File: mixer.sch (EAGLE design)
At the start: 53 parts, among them J1 SJ-3502-SMT-TR, Q1 2SCR574D3TL1, Q2 2SCR574D3TL1, U1 MCP1703T-5002E, U2 SA602AD8-SOIC, U3 LM386M-1, X1 Antenna, Y1 7.040MHz

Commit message: splitting boards, doing layouts
Split into two boards with jumpers between. Added jumper for crystal to be able to change reference frequency. Closer to real layouts, still need to solidify some parts.
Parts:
- removed C1: 0.1U, adafruit:C-USC0805
- removed C10, C12, C18: 150p, adafruit:C-USC0805
- removed C11, C16, C17, C19, C2: 10n, adafruit:C-USC0805
- removed C22: 33u/16V, adafruit:C-USC0805
- removed C23, C24, C25: 10u/16V, adafruit:C-USC0805
- removed C5: 0.1u, adafruit:C-USC0805
- removed C6, C7: 390p, adafruit:C-USC0805
- removed C8: 680p, adafruit:C-USC0805
- removed C9: 100p, adafruit:C-USC0805
- removed J1: SJ-3502-SMT-TR, Audio Connectors:SJ-3502-SMT-TR
- removed L2: 470uH, MLF2012E5R6KT000:MLF2012E5R6KT000
- removed L3: 5.6uH, MLF2012E5R6KT000:MLF2012E5R6KT000
- removed L4: 16uH, MLF2012E5R6KT000:MLF2012E5R6KT000
- removed L5: 1.2uH, MLF2012E5R6KT000:MLF2012E5R6KT000
- removed Q1, Q2: 2SCR574D3TL1, zort2:2SCR574D3TL1
- removed R1, R2: 1k, pot:TRIM_EU-3223G
- removed R6: 6.8K, adafruit:R-US_M0805
- removed R7: 100, adafruit:R-US_M0805
- removed U1: MCP1703T-5002E, linear:MCP170312MB
- removed U3: LM386M-1, linear:LM386M-1
- removed VIN: AB9V, battery:AB9V
- removed X1: Antenna, adafruit:SMACONNECTOR_EDGE
- removed Y1: 7.040MHz, adafruit:CRYSTALCTS406
- added CRYSTAL: (no value), adafruit:PINHD-1X3
- added JP1: (no value), adafruit:PINHD-2X4
- R4: value 1.5K -> 1k; device adafruit:R-US_M0805 -> zort2:3362W-1-102LF
- R5: value 6.8K -> 25K; device adafruit:R-US_M0805 -> zort2:3362W-1-102LF
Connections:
- removed net HEADPHONE: C24.2, J1.2
- removed net KEY_IN: J1.3, R4.1
- removed net N$10: C17.2, U3.-IN
- removed net N$11: C23.1, U3.BYPASS
- removed net N$12: C25.1, U3.GAIN@2
- removed net N$13: C25.2, U3.GAIN@1
- removed net N$14: C24.1, U3.OUT
- removed net N$19: C12.2, Q1.1, R5.2, R6.1
- removed net N$20: C11.1, Q1.3, R4.2
- removed net N$21: C18.1, L3.1, Q1.2
- removed net N$22: C10.1, C18.2, R7.1
- removed net N$23: L2.2, Q2.1, R7.2
- removed net N$24: C19.1, L4.1, Q2.2
- removed net N$25: C19.2, C8.1, C9.1, L5.1
- removed net N$26: C6.1, C7.1, L5.2, X1.ANT
- removed net N$9: C16.2, U3.+IN
- net 6V_DC: now also JP1.5, R5.1; no longer C2.1, R2.E, U1.VO
- net ANT_IN: now also JP1.1; no longer C9.2
- net ANT_OUT: now also JP1.2; no longer C12.1
- net GND: now also JP1.8, R4.3, R5.3; no longer C1.2, C10.2, C11.2, C2.2, C22.2, C23.2, C6.2, C7.2, C8.2, J1.1, L2.1, Q2.3, R1.A, R2.A, R5.1, U1.GND, U3.GND, VIN.-, X1.GND1, X1.GND2, X1.GND3, X1.GND4
- net N$15: now also CRYSTAL.1; no longer Y1.1
- net N$18: now also R5.2; no longer R2.S
- net N$4: now also CRYSTAL.3; no longer Y1.2
- net N$5: now also R4.2; no longer R1.S
- net N$6: now also R4.1; no longer R1.E
- net OUT_A: now also JP1.3; no longer C16.1, C5.1
- net OUT_B: now also JP1.4; no longer C17.1, C5.2
- net VIN: now also JP1.7; no longer C1.1, C22.1, L3.2, L4.2, R6.2, U1.VI1, U3.VS, VIN.+
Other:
- note added: "7.040 MHz"
- note removed: "Audio I/O"
- note removed: "Power Supply"
- moved on the sheet: C13, C14, C15, C20, C21, C26, C3, C4, D1, D2, D3, L1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

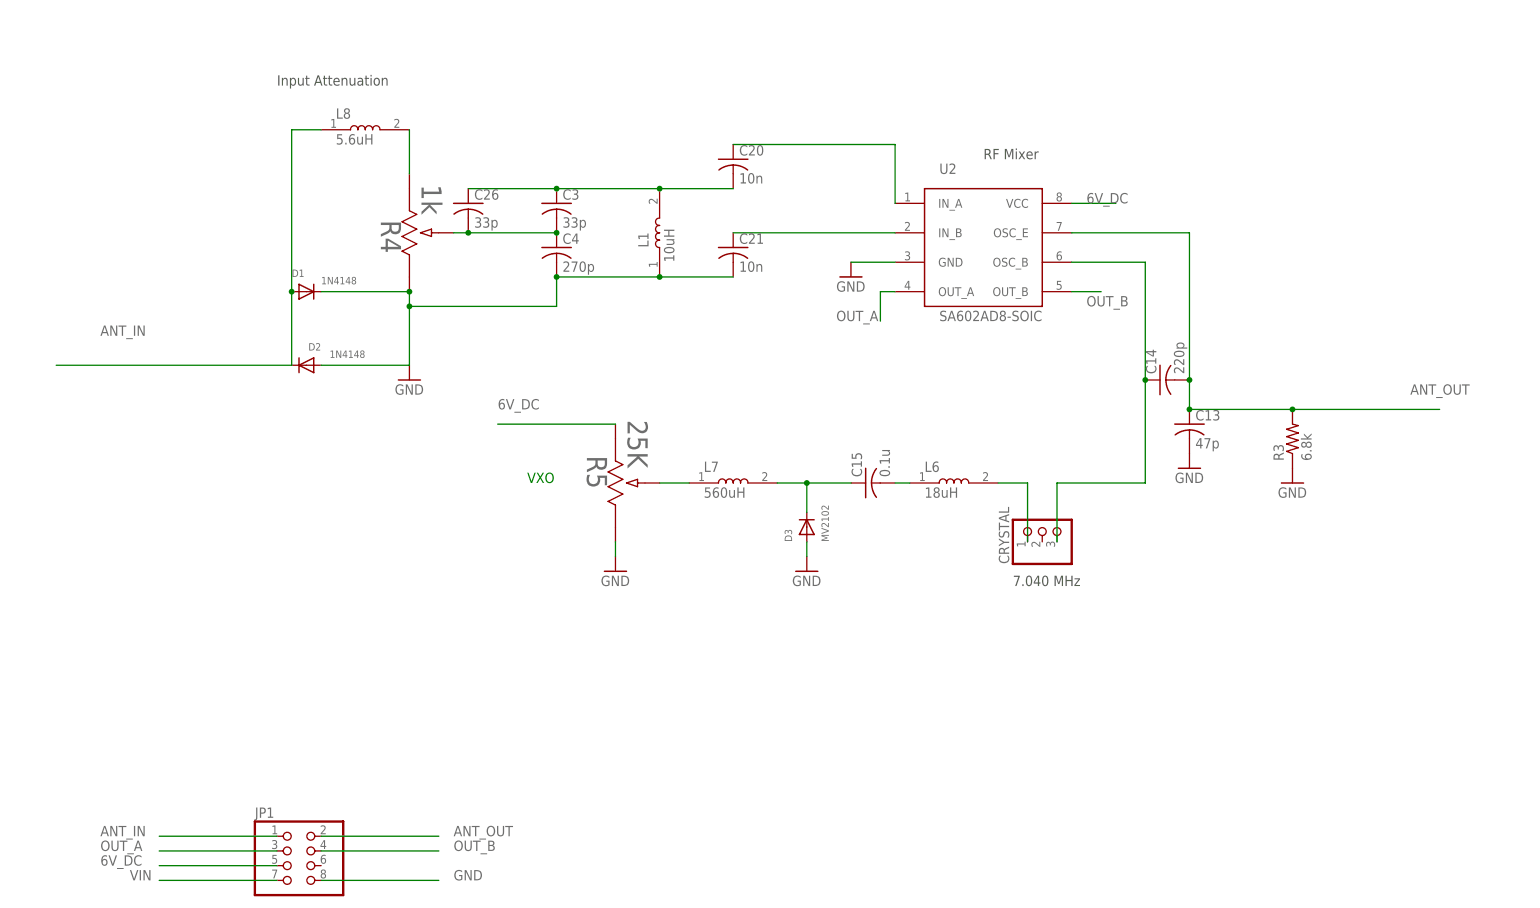
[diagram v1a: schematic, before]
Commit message: forgot to save mixer schematic
Forgot to save while adjusting the schematic layout to make it more readable
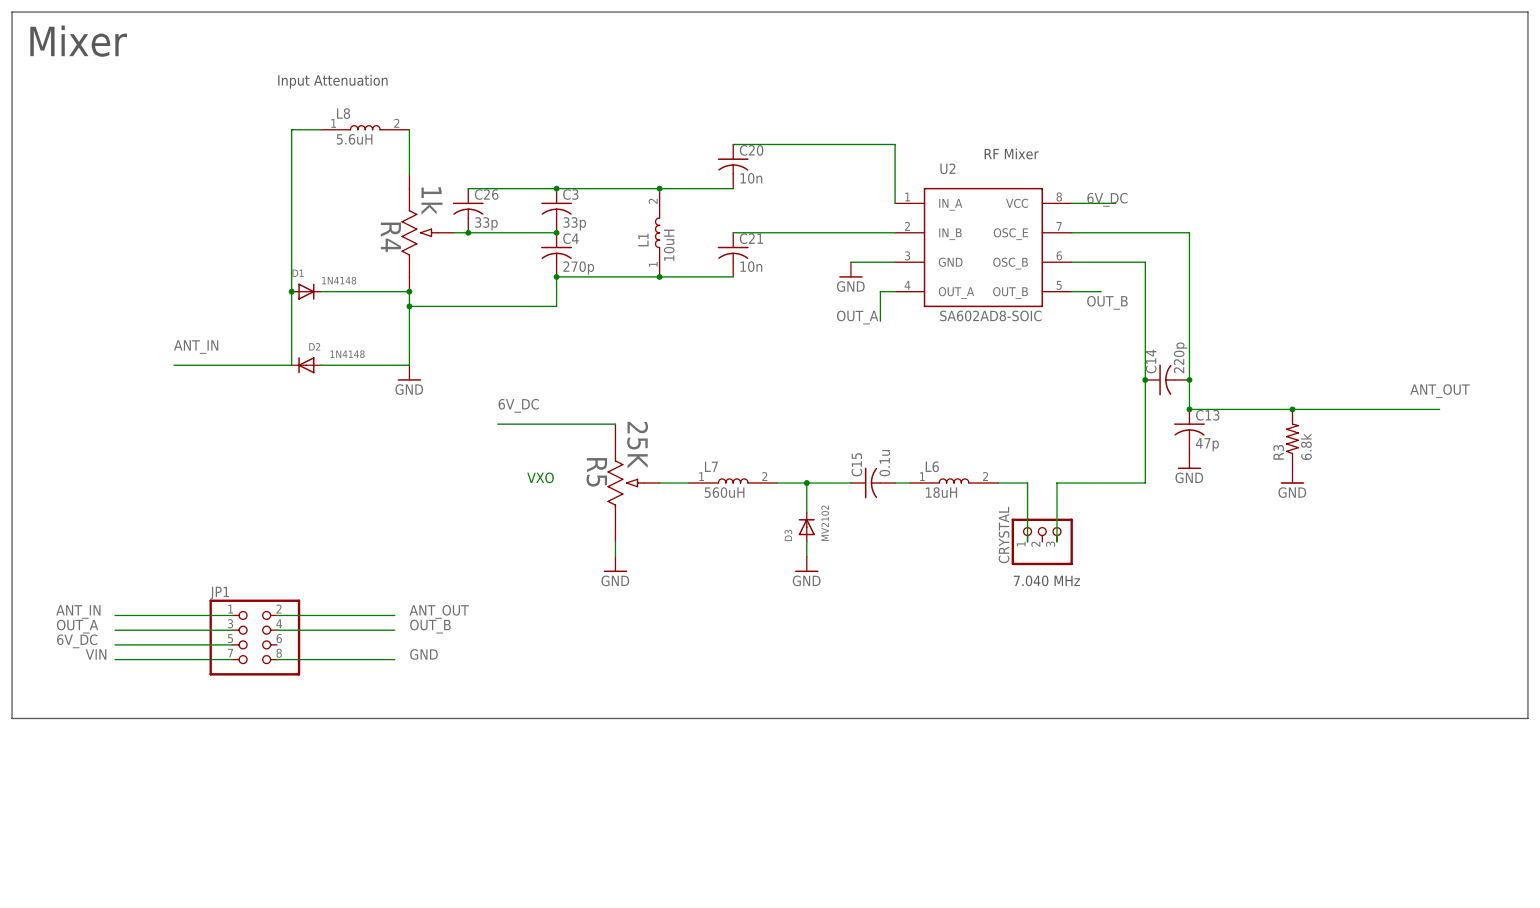
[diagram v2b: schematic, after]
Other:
- note added: "Mixer"
- moved on the sheet: JP1
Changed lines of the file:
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@@
 <text x="10.16" y="45.72" size="1.778" layer="91">VXO</text>
 <text x="93.98" y="27.94" size="1.778" layer="97">7.040 MHz</text>
+<wire x1="-78.74" y1="127" x2="-78.74" y2="5.08" width="0.1524" layer="97"/>
+<wire x1="-78.74" y1="5.08" x2="182.88" y2="5.08" width="0.1524" layer="97"/>
+<wire x1="182.88" y1="5.08" x2="182.88" y2="127" width="0.1524" layer="97"/>
+<wire x1="182.88" y1="127" x2="-78.74" y2="127" width="0.1524" layer="97"/>
+<text x="-76.2" y="119.38" size="5.08" layer="97">Mixer</text>
 </plain>
 <instances>
@@
 <attribute name="VALUE" x="55.88" y="27.94" size="1.778" layer="96"/>
 </instance>
-<instance part="JP1" gate="A" x="-30.48" y="-20.32" smashed="yes">
-<attribute name="NAME" x="-36.83" y="-12.065" size="1.778" layer="95"/>
-<attribute name="VALUE" x="-36.83" y="-27.94" size="1.778" layer="96"/>
+<instance part="JP1" gate="A" x="-38.1" y="17.78" smashed="yes">
+<attribute name="NAME" x="-44.45" y="26.035" size="1.778" layer="95"/>
+<attribute name="VALUE" x="-44.45" y="10.16" size="1.778" layer="96"/>
 </instance>
 <instance part="R4" gate="A" x="-10.16" y="99.06" smashed="yes" rot="R270">
@@
 <segment>
 <pinref part="JP1" gate="A" pin="8"/>
-<wire x1="-25.4" y1="-22.86" x2="-5.08" y2="-22.86" width="0.1524" layer="91"/>
-<label x="-2.54" y="-22.86" size="1.778" layer="95"/>
+<wire x1="-33.02" y1="15.24" x2="-12.7" y2="15.24" width="0.1524" layer="91"/>
+<label x="-10.16" y="15.24" size="1.778" layer="95"/>
 </segment>
 </net>
@@
 <segment>
 <pinref part="JP1" gate="A" pin="5"/>
-<wire x1="-33.02" y1="-20.32" x2="-53.34" y2="-20.32" width="0.1524" layer="91"/>
-<label x="-63.5" y="-20.32" size="1.778" layer="95"/>
+<wire x1="-40.64" y1="17.78" x2="-60.96" y2="17.78" width="0.1524" layer="91"/>
+<label x="-71.12" y="17.78" size="1.778" layer="95"/>
 </segment>
 </net>
@@
 <junction x="-30.48" y="78.74"/>
 <wire x1="-30.48" y1="78.74" x2="-30.48" y2="66.04" width="0.1524" layer="91"/>
-<wire x1="-30.48" y1="66.04" x2="-71.12" y2="66.04" width="0.1524" layer="91"/>
-<label x="-63.5" y="71.12" size="1.778" layer="95"/>
+<wire x1="-30.48" y1="66.04" x2="-50.8" y2="66.04" width="0.1524" layer="91"/>
+<label x="-50.8" y="68.58" size="1.778" layer="95"/>
 </segment>
 <segment>
 <pinref part="JP1" gate="A" pin="1"/>
-<wire x1="-33.02" y1="-15.24" x2="-53.34" y2="-15.24" width="0.1524" layer="91"/>
-<label x="-63.5" y="-15.24" size="1.778" layer="95"/>
+<wire x1="-40.64" y1="22.86" x2="-60.96" y2="22.86" width="0.1524" layer="91"/>
+<label x="-71.12" y="22.86" size="1.778" layer="95"/>
 </segment>
 </net>
@@
 <segment>
 <pinref part="JP1" gate="A" pin="3"/>
-<wire x1="-33.02" y1="-17.78" x2="-53.34" y2="-17.78" width="0.1524" layer="91"/>
-<label x="-63.5" y="-17.78" size="1.778" layer="95"/>
+<wire x1="-40.64" y1="20.32" x2="-60.96" y2="20.32" width="0.1524" layer="91"/>
+<label x="-71.12" y="20.32" size="1.778" layer="95"/>
 </segment>
 </net>
@@
 <segment>
 <pinref part="JP1" gate="A" pin="4"/>
-<wire x1="-25.4" y1="-17.78" x2="-5.08" y2="-17.78" width="0.1524" layer="91"/>
-<label x="-2.54" y="-17.78" size="1.778" layer="95"/>
+<wire x1="-33.02" y1="20.32" x2="-12.7" y2="20.32" width="0.1524" layer="91"/>
+<label x="-10.16" y="20.32" size="1.778" layer="95"/>
 </segment>
 </net>
@@
 <segment>
 <pinref part="JP1" gate="A" pin="2"/>
-<wire x1="-25.4" y1="-15.24" x2="-5.08" y2="-15.24" width="0.1524" layer="91"/>
-<label x="-2.54" y="-15.24" size="1.778" layer="95"/>
+<wire x1="-33.02" y1="22.86" x2="-12.7" y2="22.86" width="0.1524" layer="91"/>
+<label x="-10.16" y="22.86" size="1.778" layer="95"/>
 </segment>
 </net>
@@
 <segment>
 <pinref part="JP1" gate="A" pin="7"/>
-<wire x1="-33.02" y1="-22.86" x2="-53.34" y2="-22.86" width="0.1524" layer="91"/>
-<label x="-58.42" y="-22.86" size="1.778" layer="95"/>
-</segment>
-</net>
+<wire x1="-40.64" y1="15.24" x2="-60.96" y2="15.24" width="0.1524" layer="91"/>
+<label x="-66.04" y="15.24" size="1.778" layer="95"/>
+</segment>
+</net>

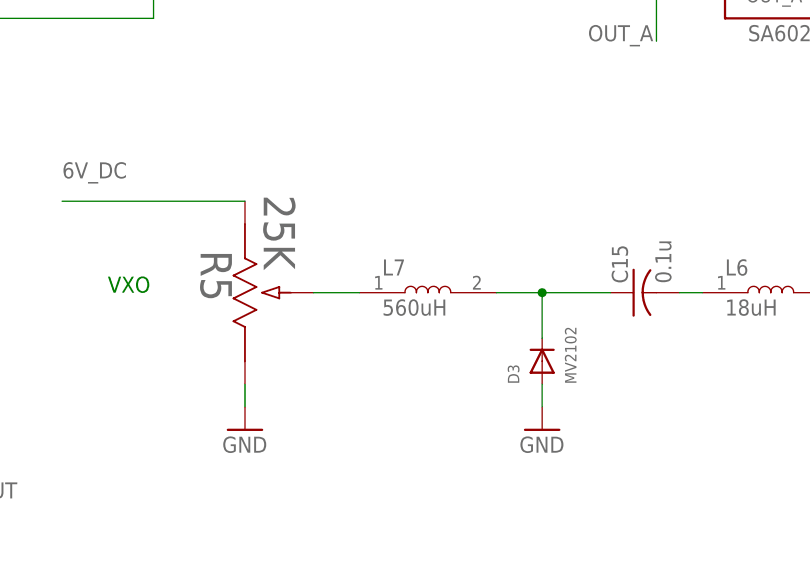
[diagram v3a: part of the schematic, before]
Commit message: Mixer board 1.1b
* fixed pad size for L7
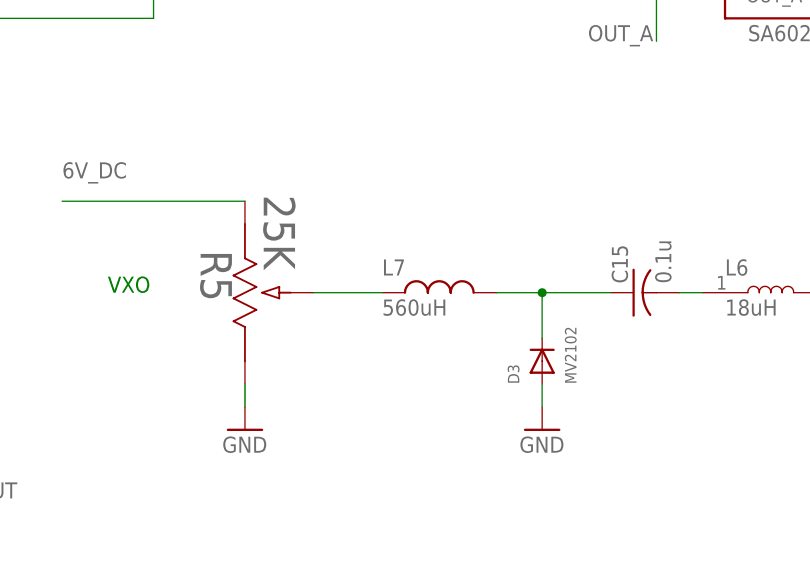
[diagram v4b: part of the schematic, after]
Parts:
- L7: device MLF2012E5R6KT000:MLF2012E5R6KT000 -> zort2:LMOLDED-1812(4532-METRIC)
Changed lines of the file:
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@@
 <part name="GND12" library="supply1" library_urn="urn:adsk.eagle:library:371" deviceset="GND" device=""/>
 <part name="L6" library="MLF2012E5R6KT000" deviceset="MLF2012E5R6KT000" device="" value="18uH"/>
-<part name="L7" library="MLF2012E5R6KT000" deviceset="MLF2012E5R6KT000" device="" value="560uH"/>
+<part name="L7" library="zort2" deviceset="L" device="" technology="MOLDED-1812(4532-METRIC)" value="560uH"/>
 <part name="GND13" library="supply1" library_urn="urn:adsk.eagle:library:371" deviceset="GND" device=""/>
 <part name="D3" library="adafruit" library_urn="urn:adsk.eagle:library:420" deviceset="DIODE" device="SOD-323F" package3d_urn="urn:adsk.eagle:package:6240873/1" value="MV2102"/>
@@
 <segment>
 <pinref part="L7" gate="G$1" pin="1"/>
-<wire x1="38.1" y1="45.72" x2="33.02" y2="45.72" width="0.1524" layer="91"/>
+<wire x1="40.64" y1="45.72" x2="33.02" y2="45.72" width="0.1524" layer="91"/>
 <pinref part="R5" gate="A" pin="2"/>
 </segment>
@@
 packages will not be understood (or retained) with this version.
 </note>
+<note version="8.4" severity="warning">
+Since Version 8.4, EAGLE supports properties for SPICE simulation.
+Probes in schematics and SPICE mapping objects found in parts and library devices
+will not be understood with this version. Update EAGLE to the latest version
+for full support of SPICE simulation.
+</note>
 </compatibility>

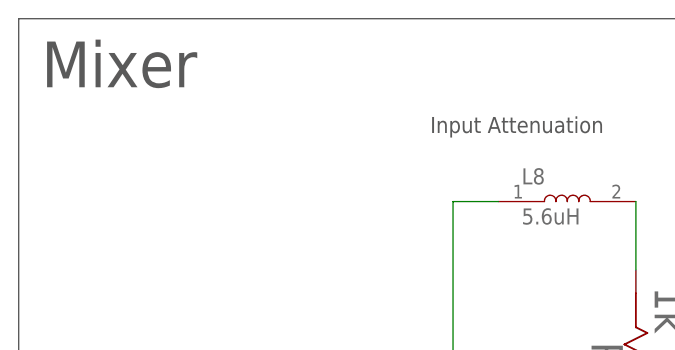
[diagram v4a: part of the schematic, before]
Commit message: Continuing on V1.1a of the I/O board
* re-placed Q1 on the layout
* updated images
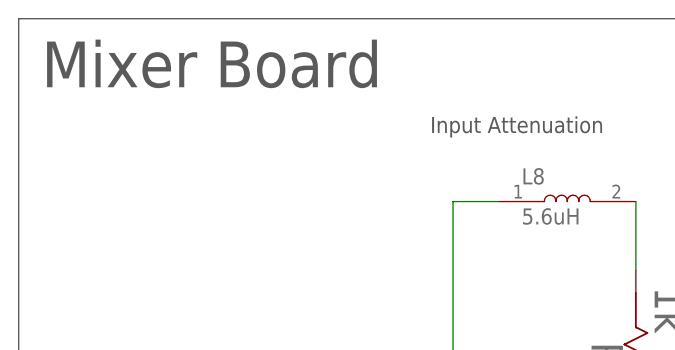
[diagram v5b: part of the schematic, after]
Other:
- note added: "Mixer Board"
- note removed: "Mixer"
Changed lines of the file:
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@@
 <?xml version="1.0" encoding="utf-8"?>
 <!DOCTYPE eagle SYSTEM "eagle.dtd">
-<eagle version="9.6.1">
+<eagle version="9.6.2">
 <drawing>
 <settings>
@@
 <wire x1="182.88" y1="5.08" x2="182.88" y2="127" width="0.1524" layer="97"/>
 <wire x1="182.88" y1="127" x2="-78.74" y2="127" width="0.1524" layer="97"/>
-<text x="-76.2" y="119.38" size="5.08" layer="97">Mixer</text>
+<text x="-76.2" y="119.38" size="5.08" layer="97">Mixer Board</text>
 </plain>
 <instances>
